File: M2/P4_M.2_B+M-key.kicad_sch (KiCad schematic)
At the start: 79 parts, among them IC1 XT25F128FWOIGT-W, IC2 TPS563202DRLR, IC4 TPS563202DRLR, J1 Micro_SD_Card_Det2, J2 USB_C_Receptacle_USB2.0_16P, Q2 MMDT2222A, U2 ESP32-P4NRW16, U5 CH340K, Y1 32KHz, Y2 40MHz

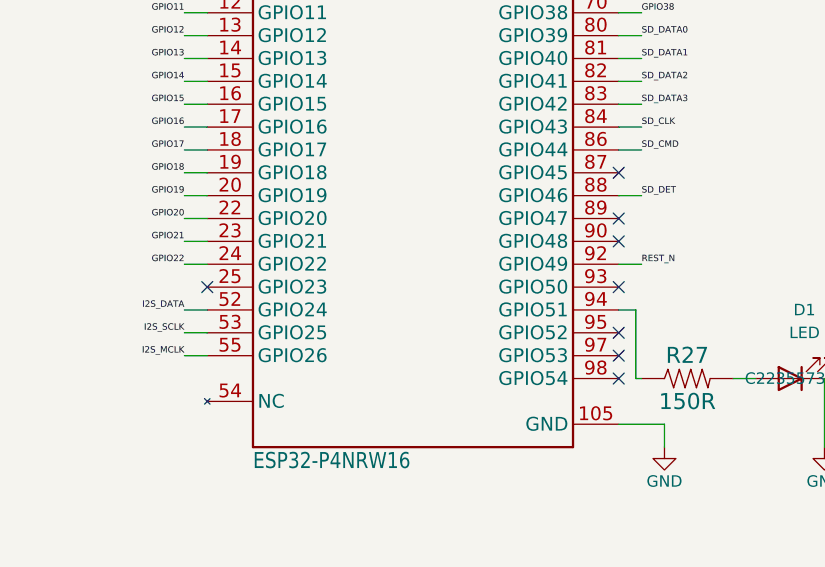
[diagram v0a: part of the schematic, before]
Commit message: fix: component positions & 3dmodels
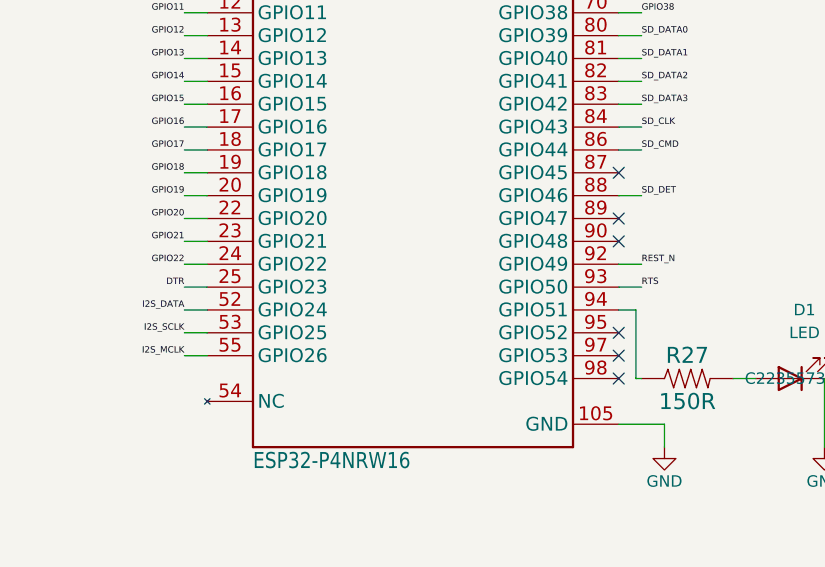
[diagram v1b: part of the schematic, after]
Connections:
- net DTR: now also U2.25 (GPIO23)
- net RTS: now also U2.93 (GPIO50)
- no-connect marks 12 -> 10
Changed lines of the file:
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@@
 	)
 	(no_connect
-		(at 132.08 149.86)
-	)
-	(no_connect
 		(at 259.08 270.51)
 	)
@@
 	)
 	(no_connect
-		(at 86.36 149.86)
-	)
-	(no_connect
 		(at 132.08 109.22)
 	)
@@
 	(wire
 		(pts
+			(xy 132.08 149.86) (xy 134.62 149.86)
+		)
+		(stroke
+			(width 0)
+			(type default)
+		)
+	)
+	(wire
+		(pts
 			(xy 320.04 370.84) (xy 320.04 375.92)
 		)
@@
 	(wire
 		(pts
+			(xy 83.82 149.86) (xy 86.36 149.86)
+		)
+		(stroke
+			(width 0)
+			(type default)
+		)
+	)
+	(wire
+		(pts
 			(xy 152.4 248.285) (xy 152.4 250.19)
 		)
@@
 		)
 	)
+	(label "RTS"
+		(at 134.62 149.86 0)
+		(effects
+			(font
+				(size 0.7112 0.7112)
+			)
+			(justify left bottom)
+		)
+	)
 	(label "3.3V"
 		(at 269.24 137.16 0)
@@
 		)
 	)
+	(label "DTR"
+		(at 83.82 149.86 180)
+		(effects
+			(font
+				(size 0.7112 0.7112)
+			)
+			(justify right bottom)
+		)
+	)

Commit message: fix: revert m2 changes
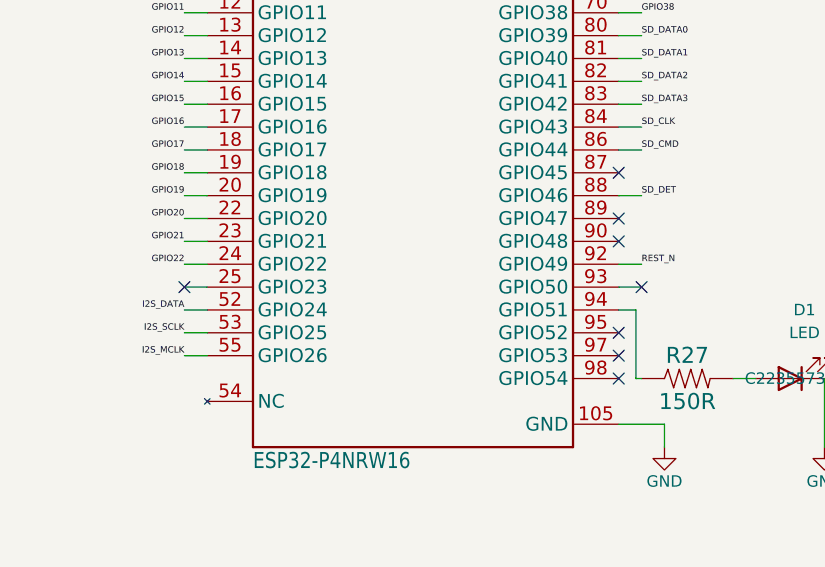
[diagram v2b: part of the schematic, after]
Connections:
- net DTR: no longer U2.25 (GPIO23)
- net RTS: no longer U2.93 (GPIO50)
- no-connect marks 10 -> 12
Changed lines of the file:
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@@
 	)
 	(no_connect
+		(at 134.62 149.86)
+	)
+	(no_connect
 		(at 259.08 270.51)
 	)
 	(no_connect
+		(at 83.82 149.86)
+	)
+	(no_connect
 		(at 132.08 160.02)
 	)
@@
 		)
 	)
-	(label "RTS"
-		(at 134.62 149.86 0)
-		(effects
-			(font
-				(size 0.7112 0.7112)
-			)
-			(justify left bottom)
-		)
-	)
 	(label "3.3V"
 		(at 269.24 137.16 0)
@@
 		)
 	)
-	(label "DTR"
-		(at 83.82 149.86 180)
-		(effects
-			(font
-				(size 0.7112 0.7112)
-			)
-			(justify right bottom)
-		)
-	)

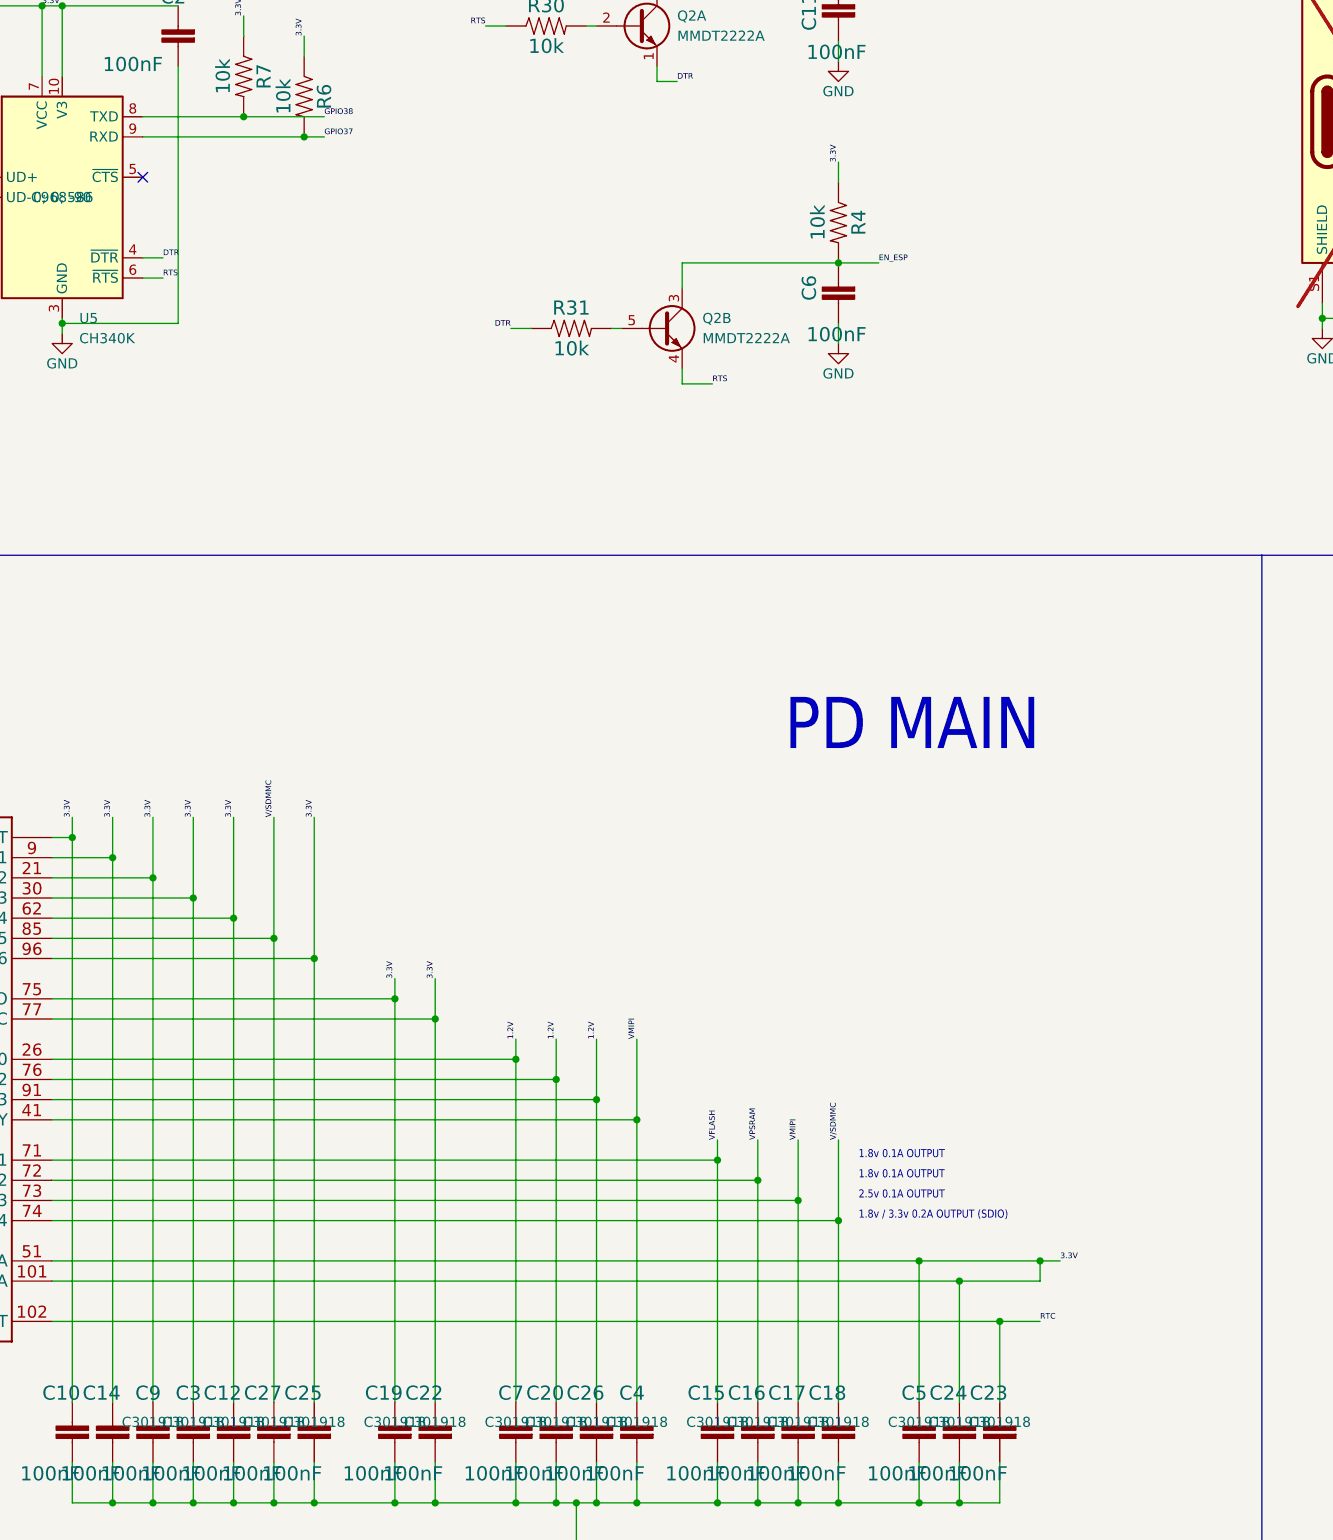
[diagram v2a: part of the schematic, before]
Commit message: Fixed esp_en issue
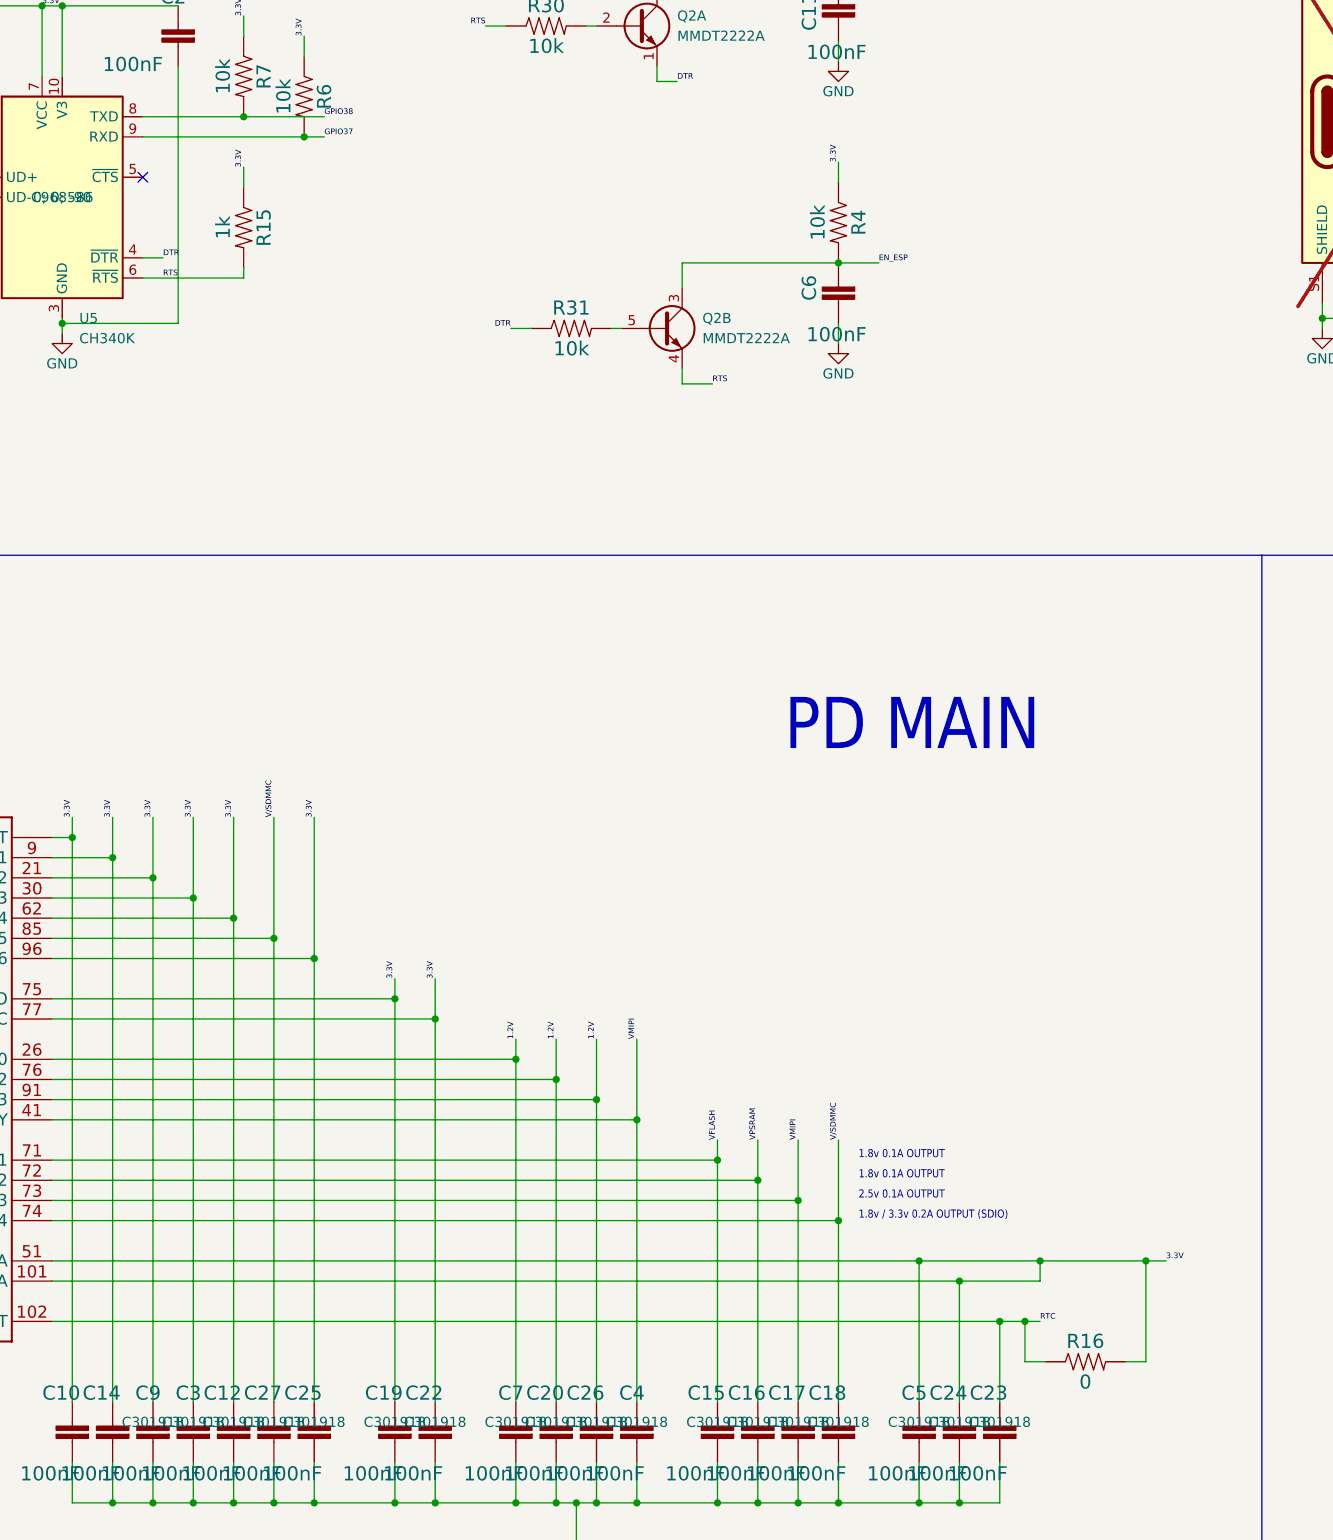
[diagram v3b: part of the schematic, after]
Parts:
- added R15: 1k, Resistor_SMD:R_0201_0603Metric, symbol P4_M.2_B+M-key-eagle-import:RESISTOR-0201-1/4W-1%
- added R16: 0, Resistor_SMD:R_0201_0603Metric, symbol P4_M.2_B+M-key-eagle-import:RESISTOR-0201-1/4W-1%
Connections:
- net 3.3V: now also R15.1, R16.2
- net RTC: now also R16.1
- net RTS: now also R15.2
